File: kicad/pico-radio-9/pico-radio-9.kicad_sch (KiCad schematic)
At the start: 58 parts, among them J1 FM antenna, J2 SW antenna, J3 MW/SW antenna kapcsoló, J4 HF Amplifier, J5 Batterry, Q1 PN2222A, Q2 PN2222A, Q3 PN2222A, SW1 Reset, U1 SI4732-A10-GS, U2 TFT_320x240, U3 MCP6004, U4 KY-040, Y1 32.762kHz

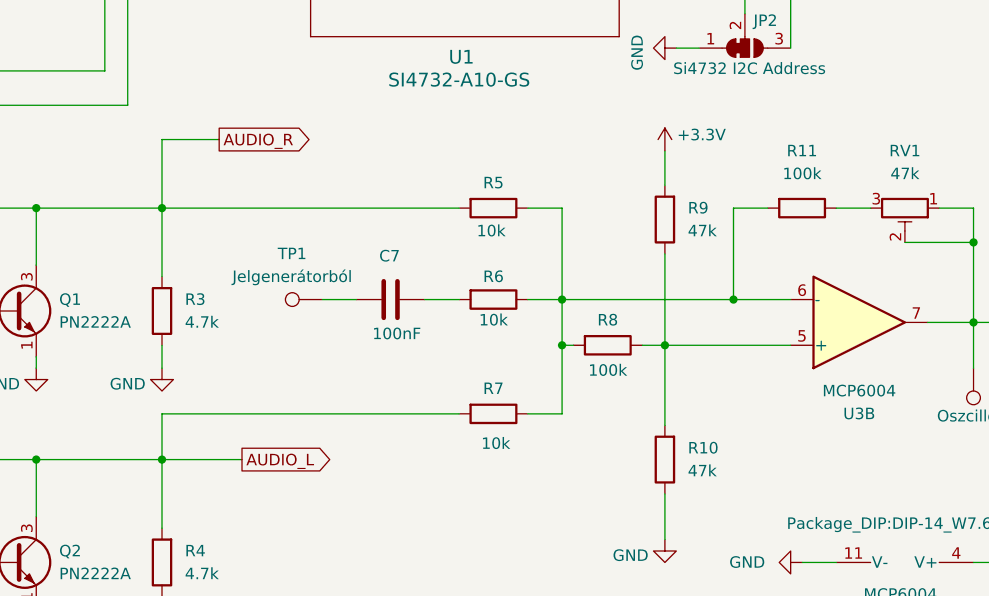
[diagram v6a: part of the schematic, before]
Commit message: Add capacitors C13 and C14 to the schematic and update connections
- Added capacitor C13 (100nF) at coordinates (96.52, 148.59) with appropriate properties.
- Added capacitor C14 (100nF) at coordinates (96.52, 171.45) with appropriate properties.
- Updated wire connections for C13 and C14.
- Changed the value of resistor R1 from 100k to 47k.
- Adjusted the position of capacitor C7 for better layout.
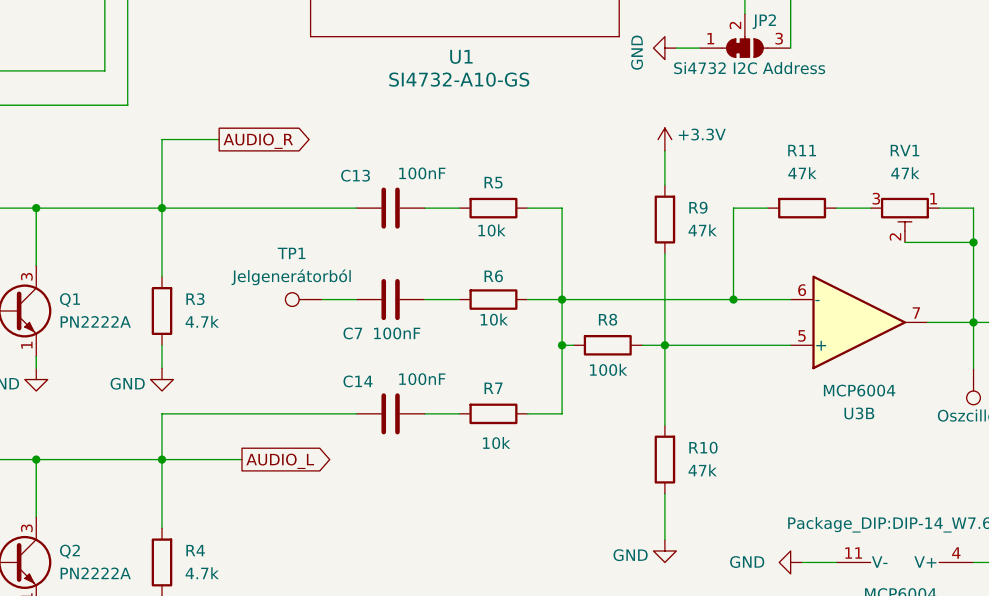
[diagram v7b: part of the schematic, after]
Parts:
- added C13, C14: 100nF, Capacitor_THT:C_Disc_D7.0mm_W2.5mm_P5.00mm, symbol Device:C
- R11: value 100k -> 47k
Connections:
- net AUDIO_L: now also C14.2; no longer R7.2
- net AUDIO_R: now also C13.2; no longer R5.2
- new net: C14.1, R7.2
- new net: C13.1, R5.2
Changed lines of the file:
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@@
 	(wire
 		(pts
+			(xy 71.12 148.59) (xy 92.71 148.59)
+		)
+		(stroke
+			(width 0)
+			(type default)
+		)
+	)
+	(wire
+		(pts
 			(xy 182.88 102.87) (xy 185.42 102.87)
 		)
@@
 	(wire
 		(pts
+			(xy 100.33 171.45) (xy 104.14 171.45)
+		)
+		(stroke
+			(width 0)
+			(type default)
+		)
+	)
+	(wire
+		(pts
 			(xy 250.19 96.52) (xy 254 96.52)
 		)
@@
 	(wire
 		(pts
+			(xy 71.12 171.45) (xy 92.71 171.45)
+		)
+		(stroke
+			(width 0)
+			(type default)
+		)
+	)
+	(wire
+		(pts
 			(xy 161.29 148.59) (xy 161.29 152.4)
 		)
@@
 		)
 	)
-	(wire
-		(pts
-			(xy 71.12 148.59) (xy 104.14 148.59)
-		)
-		(stroke
-			(width 0)
-			(type default)
-		)
-	)
 	(bus
 		(pts
@@
 	(wire
 		(pts
-			(xy 71.12 171.45) (xy 104.14 171.45)
-		)
-		(stroke
-			(width 0)
-			(type default)
-		)
-	)
-	(wire
-		(pts
 			(xy 93.98 62.23) (xy 93.98 71.12)
 		)
@@
 	(wire
 		(pts
+			(xy 100.33 148.59) (xy 104.14 148.59)
+		)
+		(stroke
+			(width 0)
+			(type default)
+		)
+	)
+	(wire
+		(pts
 			(xy 232.41 73.66) (xy 232.41 76.2)
 		)
@@
 			)
 		)
-		(property "Value" "100k"
+		(property "Value" "47k"
 			(at 142.24 144.78 90)
 			(effects
@@
 		(dnp no)
 		(property "Reference" "C7"
-			(at 95.25 153.924 90)
+			(at 91.186 162.56 90)
 			(effects
 				(font
@@
 	)
 	(symbol
+		(lib_id "Device:C")
+		(at 96.52 148.59 270)
+		(unit 1)
+		(exclude_from_sim no)
+		(in_bom yes)
+		(on_board yes)
+		(dnp no)
+		(property "Reference" "C13"
+			(at 90.932 145.034 90)
+			(effects
+				(font
+					(size 1.27 1.27)
+				)
+				(justify left)
+			)
+		)
+		(property "Value" "100nF"
+			(at 97.282 144.78 90)
+			(effects
+				(font
+					(size 1.27 1.27)
+				)
+				(justify left)
+			)
+		)
+		(property "Footprint" "Capacitor_THT:C_Disc_D7.0mm_W2.5mm_P5.00mm"
+			(at 92.71 149.5552 0)
+			(effects
+				(font
+					(size 1.27 1.27)
+				)
+				(hide yes)
+			)
+		)
+		(property "Datasheet" "~"
+			(at 96.52 148.59 0)
+			(effects
+				(font
+					(size 1.27 1.27)
+				)
+				(hide yes)
+			)
+		)
+		(property "Description" "Unpolarized capacitor"
+			(at 96.52 148.59 0)
+			(effects
+				(font
+					(size 1.27 1.27)
+				)
+				(hide yes)
+			)
+		)
+		(pin "1"
+		)
+		(pin "2"
+		)
+		(instances
+			(project "pico-radio-9"
+				(path "/b9640508-dcc6-4f6b-830f-c53a732dcb5b"
+					(reference "C13")
+					(unit 1)
+				)
+			)
+		)
+	)
+	(symbol
 		(lib_id "power:GND")
 		(at 232.41 87.63 0)
@@
 					(unit 1)
 				)
+			)
+		)
+	)
+	(symbol
+		(lib_id "Device:C")
+		(at 96.52 171.45 270)
+		(unit 1)
+		(exclude_from_sim no)
+		(in_bom yes)
+		(on_board yes)
+		(dnp no)
+		(property "Reference" "C14"
+			(at 91.186 167.894 90)
+			(effects
+				(font
+					(size 1.27 1.27)
+				)
+				(justify left)
+			)
+		)
+		(property "Value" "100nF"
+			(at 97.282 167.64 90)
+			(effects
+				(font
+					(size 1.27 1.27)
+				)
+				(justify left)
+			)
+		)
+		(property "Footprint" "Capacitor_THT:C_Disc_D7.0mm_W2.5mm_P5.00mm"
+			(at 92.71 172.4152 0)
+			(effects
+				(font
+					(size 1.27 1.27)
+				)
+				(hide yes)
+			)
+		)
+		(property "Datasheet" "~"
+			(at 96.52 171.45 0)
+			(effects
+				(font
+					(size 1.27 1.27)
+				)
+				(hide yes)
+			)
+		)
+		(property "Description" "Unpolarized capacitor"
+			(at 96.52 171.45 0)
+			(effects
+				(font
+					(size 1.27 1.27)
+				)
+				(hide yes)
+			)
+		)
+		(pin "1"
+		)
+		(pin "2"
+		)
+		(instances
+			(project "pico-radio-9"
+				(path "/b9640508-dcc6-4f6b-830f-c53a732dcb5b"
+					(reference "C14")
+					(unit 1)
+				)
